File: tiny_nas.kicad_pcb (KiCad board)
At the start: 4 copper layers, 0 parts

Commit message: pcb component placement
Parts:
- added C1: 100n, Capacitor_SMD:C_0402_1005Metric, F.Cu at (128.8, 95.5)
- added C10: 100n, Capacitor_SMD:C_0402_1005Metric, F.Cu at (144.8, 73.4)
- added C11: 100n, Capacitor_SMD:C_0402_1005Metric, F.Cu at (137.9, 73.9)
- added C12: 100n, Capacitor_SMD:C_0402_1005Metric, F.Cu at (127.5, 93.0)
- added C13: 100n, Capacitor_SMD:C_0402_1005Metric, F.Cu at (132.1, 96.5)
- added C14: 22u, Capacitor_SMD:C_0805_2012Metric, F.Cu at (171.7, 124.2)
- added C15: 100n, Capacitor_SMD:C_0402_1005Metric, F.Cu at (130.0, 83.3)
- added C16: 100n, Capacitor_SMD:C_0402_1005Metric, F.Cu at (131.6, 88.1)
- added C17: 22u, Capacitor_SMD:C_0805_2012Metric, F.Cu at (172.5, 118.4)
- added C18: 100n, Capacitor_SMD:C_0402_1005Metric, F.Cu at (132.1, 94.5)
- added C19: 100n, Capacitor_SMD:C_0402_1005Metric, F.Cu at (139.7, 103.6)
- added C2: 4.7u, Capacitor_SMD:C_0603_1608Metric, F.Cu at (130.0, 82.0)
- added C20: 100n, Capacitor_SMD:C_0402_1005Metric, F.Cu at (146.1, 103.6)
- added C21: 100n, Capacitor_SMD:C_0402_1005Metric, F.Cu at (151.1, 103.9)
- added C22: 10p, Capacitor_SMD:C_0402_1005Metric, F.Cu at (121.7, 93.0)
- added C23: 10p, Capacitor_SMD:C_0402_1005Metric, F.Cu at (121.7, 91.4)
- added C24: 30p, Capacitor_SMD:C_0402_1005Metric, F.Cu at (103.6, 89.9)
- added C25: 30p, Capacitor_SMD:C_0402_1005Metric, F.Cu at (103.6, 80.8)
- added C26: 100n, Capacitor_SMD:C_0402_1005Metric, F.Cu at (124.5, 85.3)
- added C27: 470p, Capacitor_SMD:C_0402_1005Metric, F.Cu at (117.9, 80.8)
- added C28: 100n, Capacitor_SMD:C_0402_1005Metric, F.Cu at (146.3, 120.6)
- added C29: 1u, Capacitor_SMD:C_0603_1608Metric, F.Cu at (117.9, 81.8)
- added C3: 2.2u, Capacitor_SMD:C_0603_1608Metric, F.Cu at (155.7, 104.9)
- added C30: 4.7u, Capacitor_SMD:C_0603_1608Metric, F.Cu at (147.1, 107.7)
- added C31: 100n, Capacitor_SMD:C_0402_1005Metric, F.Cu at (128.5, 76.7)
- added C32: 100n, Capacitor_SMD:C_0402_1005Metric, F.Cu at (118.1, 77.0)
- added C33: 100n, Capacitor_SMD:C_0402_1005Metric, F.Cu at (142.7, 108.5)
- added C34: 100n, Capacitor_SMD:C_0402_1005Metric, F.Cu at (140.5, 108.7)
- added C35: 10u, Capacitor_SMD:C_0805_2012Metric, F.Cu at (114.6, 74.2)
- added C36: 100n, Capacitor_SMD:C_0402_1005Metric, F.Cu at (151.4, 120.1)
- added C37: 100n, Capacitor_SMD:C_0402_1005Metric, F.Cu at (149.6, 108.7)
- added C38: 4.7u, Capacitor_SMD:C_0603_1608Metric, F.Cu at (139.2, 108.7)
- added C39: 100n, Capacitor_SMD:C_0402_1005Metric, F.Cu at (147.8, 120.1)
- added C4: 100n, Capacitor_SMD:C_0402_1005Metric, F.Cu at (158.8, 101.9)
- added C40: 100n, Capacitor_SMD:C_0402_1005Metric, F.Cu at (136.1, 114.6)
- added C41: 100n, Capacitor_SMD:C_0402_1005Metric, F.Cu at (110.5, 72.6)
- added C42: 100n, Capacitor_SMD:C_0402_1005Metric, F.Cu at (142.0, 68.3)
- added C43: 100n, Capacitor_SMD:C_0402_1005Metric, F.Cu at (134.4, 70.4)
- added C44: 100n, Capacitor_SMD:C_0402_1005Metric, F.Cu at (113.8, 70.1)
- added C45: 100n, Capacitor_SMD:C_0402_1005Metric, F.Cu at (173.5, 115.8)
- added C46: 100n, Capacitor_SMD:C_0402_1005Metric, F.Cu at (168.4, 109.0)
- added C47: 4.7u, Capacitor_SMD:C_0603_1608Metric, F.Cu at (159.0, 118.6)
- added C48: 4.7u, Capacitor_SMD:C_0603_1608Metric, F.Cu at (162.3, 115.8)
- added C49: 33p, Capacitor_SMD:C_0402_1005Metric, F.Cu at (153.4, 108.7)
- added C5: 2.2u, Capacitor_SMD:C_0603_1608Metric, F.Cu at (163.8, 80.5)
- added C50: 33p, Capacitor_SMD:C_0402_1005Metric, F.Cu at (162.8, 108.7)
- added C6: 100n, Capacitor_SMD:C_0402_1005Metric, F.Cu at (163.3, 92.2)
- added C7: 100n, Capacitor_SMD:C_0402_1005Metric, F.Cu at (163.3, 86.9)
- added C8: 100n, Capacitor_SMD:C_0402_1005Metric, F.Cu at (160.5, 77.2)
- added C9: 100n, Capacitor_SMD:C_0402_1005Metric, F.Cu at (150.4, 73.4)
- added D1: LED, LED_SMD:LED_0603_1608Metric, F.Cu at (159.5, 124.5)
- added D2: LED, LED_SMD:LED_0603_1608Metric, F.Cu at (169.9, 101.6)
- added FB1: 600R, Inductor_SMD:L_0603_1608Metric, F.Cu at (138.7, 63.2)
- added FB2: 120R, Inductor_SMD:L_0603_1608Metric, F.Cu at (169.2, 92.5)
- added FB3: 120R, Inductor_SMD:L_0603_1608Metric, F.Cu at (133.9, 122.9)
- added J1: Conn_02x07_Odd_Even, Connector_PinHeader_1.27mm:PinHeader_2x07_P1.27mm_Vertical, F.Cu at (173.2, 61.7)
- added J2: DM3AT-SF-PEJM5, DM3AT-SF-PEJM5:HRS_DM3AT-SF-PEJM5, F.Cu at (113.0, 109.0)
- added J3: USB_B_Micro, Connector_USB:USB_Micro-B_Molex_47346-0001, F.Cu at (174.9, 87.4)
- added J4: Conn_01x02_Male, Connector_PinHeader_2.54mm:PinHeader_1x02_P2.54mm_Vertical, F.Cu at (124.7, 121.2)
- added J5: HR911105A, HR911105A:HANRUN_HR911105A, F.Cu at (124.0, 62.0)
- added J6: USB_B_Micro, Connector_USB:USB_Micro-B_Molex_47346-0001, F.Cu at (143.8, 124.2)
- added J7: USB_B_Micro, Connector_USB:USB_Micro-B_Molex_47346-0001, F.Cu at (175.0, 110.0)
- added J8: Conn_01x02_Male, Connector_PinHeader_2.54mm:PinHeader_1x02_P2.54mm_Vertical, F.Cu at (172.7, 78.0)
- added J9: Conn_01x02_Male, Connector_PinHeader_2.54mm:PinHeader_1x02_P2.54mm_Vertical, F.Cu at (151.6, 125.0)
- added JP1: SolderJumper_2_Bridged, Jumper:SolderJumper-2_P1.3mm_Bridged_RoundedPad1.0x1.5mm, F.Cu at (145.0, 107.7)
- added JP2: SolderJumper_2_Bridged, Jumper:SolderJumper-2_P1.3mm_Bridged_RoundedPad1.0x1.5mm, F.Cu at (145.5, 118.5)
- added R1: 4.7k, Resistor_SMD:R_0402_1005Metric, F.Cu at (158.5, 60.5)
- added R10: 33R, Resistor_SMD:R_0402_1005Metric, F.Cu at (125.2, 101.3)
- added R11: 33R, Resistor_SMD:R_0402_1005Metric, F.Cu at (128.3, 104.9)
- added R12: 33R, Resistor_SMD:R_0402_1005Metric, F.Cu at (128.3, 101.3)
- added R13: 33R, Resistor_SMD:R_0402_1005Metric, F.Cu at (131.1, 101.3)
- added R14: 0R, Resistor_SMD:R_0402_1005Metric, F.Cu at (131.1, 104.9)
- added R15: 47k, Resistor_SMD:R_0402_1005Metric, F.Cu at (116.1, 103.4)
- added R16: 47k, Resistor_SMD:R_0402_1005Metric, F.Cu at (113.0, 103.4)
- added R17: 47k, Resistor_SMD:R_0402_1005Metric, F.Cu at (110.0, 103.4)
- added R18: 47k, Resistor_SMD:R_0402_1005Metric, F.Cu at (106.9, 103.4)
- added R19: 100R, Resistor_SMD:R_0402_1005Metric, F.Cu at (108.5, 99.6)
- added R2: 1k5, Resistor_SMD:R_0402_1005Metric, F.Cu at (175.5, 121.9)
- added R20: 47k, Resistor_SMD:R_0402_1005Metric, F.Cu at (104.1, 103.4)
- added R21: 12.1k, Resistor_SMD:R_0402_1005Metric, F.Cu at (104.4, 99.6)
- added R22: 50R, Resistor_SMD:R_0402_1005Metric, F.Cu at (111.5, 78.5)
- added R23: 10k, Resistor_SMD:R_0402_1005Metric, F.Cu at (128.8, 85.6)
- added R24: 50R, Resistor_SMD:R_0402_1005Metric, F.Cu at (111.8, 81.0)
- added R25: 50R, Resistor_SMD:R_0402_1005Metric, F.Cu at (114.0, 86.6)
- added R26: 270R, Resistor_SMD:R_0402_1005Metric, F.Cu at (112.5, 55.1)
- added R27: 270R, Resistor_SMD:R_0402_1005Metric, F.Cu at (136.7, 55.4)
- added R28: 50R, Resistor_SMD:R_0402_1005Metric, F.Cu at (112.8, 83.8)
- added R29: 12k, Resistor_SMD:R_0402_1005Metric, F.Cu at (126.0, 109.7)
- added R3: 1k5, Resistor_SMD:R_0402_1005Metric, F.Cu at (173.2, 101.6)
- added R30: 820R, Resistor_SMD:R_0402_1005Metric, F.Cu at (133.3, 119.1)
- added R31: 100k, Resistor_SMD:R_0402_1005Metric, F.Cu at (159.3, 117.1)
- added R32: 1M, Resistor_SMD:R_0402_1005Metric, F.Cu at (159.0, 109.2)
- added R33: 0R, Resistor_SMD:R_0402_1005Metric, F.Cu at (135.4, 111.5)
- added R4: 10k, Resistor_SMD:R_0402_1005Metric, F.Cu at (104.9, 93.0)
- added R5: 10k, Resistor_SMD:R_0402_1005Metric, F.Cu at (107.7, 93.0)
- added R6: 10k, Resistor_SMD:R_0402_1005Metric, F.Cu at (110.7, 93.0)
- added R7: 1k5, Resistor_SMD:R_0402_1005Metric, F.Cu at (106.4, 96.0)
- added R8: 10k, Resistor_SMD:R_0402_1005Metric, F.Cu at (109.5, 96.0)
- added R9: 10k, Resistor_SMD:R_0402_1005Metric, F.Cu at (153.7, 71.9)
- added SW1: SW_SPDT, Button_Switch_SMD:SW_SPDT_PCM12, F.Cu at (168.1, 54.4)
- added U1: AMS1117-3.3, Package_TO_SOT_SMD:SOT-223-3_TabPin2, F.Cu at (165.6, 121.2)
- added U2: LAN8720A, Package_DFN_QFN:QFN-24-1EP_4x4mm_P0.5mm_EP2.6x2.6mm, F.Cu at (124.7, 80.5)
- added U3: STM32F407ZGTx, Package_QFP:LQFP-144_20x20mm_P0.5mm, F.Cu at (147.3, 88.9)
- added U4: USBLC6-4SC6, Package_TO_SOT_SMD:SOT-23-6, F.Cu at (105.3, 75.9)
- added U5: USB3300-EZK, Package_DFN_QFN:QFN-32-1EP_5x5mm_P0.5mm_EP3.45x3.45mm, F.Cu at (143.5, 113.9)
- added U6: MAX1823BEUB, MAX1823BEUB_T:SOP50P490X110-10N, F.Cu at (151.1, 117.3)
- added U7: CH340E, Package_SO:MSOP-10_3x3mm_P0.5mm, F.Cu at (168.3, 113.0)
- added Y1: 16MHz, Crystal:Crystal_SMD_3225-4Pin_3.2x2.5mm, F.Cu at (117.6, 92.2)
- added Y2: 25MHz, Crystal:Crystal_HC49-U_Vertical, F.Cu at (106.7, 87.8)
- added Y3: 24MHz, Crystal:Crystal_HC49-U_Vertical, F.Cu at (154.3, 112.5)
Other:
- board outline added: 76.2 x 76.2 mm

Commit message: route USB3300
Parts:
- moved R3 40.1 mm to (167.1, 62.0)
- moved D2 40.1 mm to (163.8, 62.0)
- moved U6 24.6 mm to (167.9, 99.3)
- moved C49 24.1 mm to (177.0, 104.1), turned to -90 degrees
- moved Y3 22.5 mm to (174.0, 101.8), turned to 90 degrees
- moved C50 20.7 mm to (176.8, 93.5), turned to 90 degrees
- moved U4 19.5 mm to (124.7, 74.4)
- moved R2 19.0 mm to (156.7, 124.5)
- moved JP2 18.9 mm to (162.3, 109.7)
- moved FB1 16.6 mm to (131.1, 78.0), turned to 90 degrees
- moved JP1 14.5 mm to (159.5, 109.0), turned to 180 degrees
- moved C30 12.8 mm to (159.5, 110.7), turned to 180 degrees
- moved R32 11.7 mm to (169.9, 105.2), turned to 90 degrees
- moved C28 8.67 mm to (154.9, 119.9)
- moved C39 3.09 mm to (149.1, 123.0)
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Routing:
- net +3V3: track 0.00 -> 187.1 mm, vias 0 -> 3
- net /ULPI_RESET: track 0.00 -> 69.5 mm
- net Net-(R31-Pad1): track 0.00 -> 69.4 mm, vias 0 -> 8
- net Net-(U5-Pad3): track 0.00 -> 60.0 mm, vias 0 -> 2
- net /ULPI_STP: track 0.00 -> 59.3 mm, vias 0 -> 2
- net Net-(J4-Pad1): track 0.00 -> 56.5 mm, vias 0 -> 4
- net Net-(R30-Pad1): track 0.00 -> 56.1 mm, vias 0 -> 6
- net /ULPI_DIR: track 0.00 -> 55.4 mm, vias 0 -> 2
- net /ULPI_D7: track 0.00 -> 55.0 mm, vias 0 -> 2
- net /ULPI_NXT: track 0.00 -> 52.4 mm, vias 0 -> 2
- net GND: track 0.00 -> 49.0 mm, vias 0 -> 9
- net /ETH_TX-: track 0.00 -> 48.0 mm
- net Net-(C50-Pad1): track 0.00 -> 47.0 mm, vias 0 -> 6
- net /ETH_TX+: track 0.00 -> 45.4 mm
- net Net-(C49-Pad1): track 0.00 -> 44.4 mm, vias 0 -> 6
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- added copper zone on In1.Cu, net GND
- added copper zone on In2.Cu, net GND

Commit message: route all
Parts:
- moved R19 65.9 mm to (166.6, 68.6)
- moved R9 32.5 mm to (125.2, 87.6), turned to 180 degrees
- moved R28 30.9 mm to (139.2, 67.8), turned to 180 degrees
- moved R25 29.9 mm to (138.4, 69.3), turned to 180 degrees
- moved R11 21.4 mm to (110.2, 93.5), turned to 180 degrees
- moved R14 19.3 mm to (113.8, 96.3)
- moved R24 13.0 mm to (111.0, 68.1)
- moved R22 12.7 mm to (111.0, 65.8)
- moved R23 10.0 mm to (118.9, 87.1)
- moved C43 6.18 mm to (135.4, 76.5)
- moved C50 4.07 mm to (177.0, 97.5), turned to -90 degrees
- moved R12 3.87 mm to (126.7, 97.8), turned to 180 degrees
- moved C49 3.56 mm to (177.0, 100.6), turned to 90 degrees
- moved C37 3.06 mm to (147.3, 110.7)
- moved C11 2.18 mm to (139.7, 75.2)
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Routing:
- net +3V3: track 187.1 -> 542.6 mm, vias 3 -> 26
- net Net-(U3-Pad114): track 0.00 -> 139.1 mm, vias 0 -> 4
- net GND: track 49.0 -> 178.5 mm, vias 9 -> 59
- net Net-(C31-Pad1): track 0.00 -> 118.6 mm, vias 0 -> 4
- net Net-(C12-Pad2): track 0.00 -> 92.8 mm, vias 0 -> 8
- net Net-(J5-Pad9): track 0.00 -> 91.5 mm, vias 0 -> 2
- net /SDIO_CK: track 0.00 -> 77.1 mm, vias 0 -> 6
- net /USART_RX: track 0.00 -> 74.3 mm, vias 0 -> 4
- net /SDIO_CMD: track 0.00 -> 72.7 mm, vias 0 -> 8
- net Net-(J5-Pad12): track 0.00 -> 72.7 mm, vias 0 -> 2
- net /SDIO_D1: track 0.00 -> 71.7 mm, vias 0 -> 4
- net /SDIO_D0: track 0.00 -> 68.9 mm, vias 0 -> 6
- net /SDIO_D3: track 0.00 -> 68.4 mm, vias 0 -> 6
- net /USART_TX: track 0.00 -> 68.3 mm, vias 0 -> 8
- net Net-(U3-Pad115): track 0.00 -> 68.1 mm, vias 0 -> 2
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
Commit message: passed DRC
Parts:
- moved C49 7.98 mm to (175.8, 92.7), turned to 180 degrees
- moved C50 6.48 mm to (172.7, 92.7), turned to 0 degrees
- moved C24 2.58 mm to (103.4, 92.5)
- moved C25 2.54 mm to (105.2, 78.7), turned to 0 degrees
- moved R6 1.14 mm to (111.3, 92.2)
- moved C1 0.76 mm to (128.8, 96.3)
- moved C36 0.38 mm to (151.6, 119.9), turned to 180 degrees
- moved C30 0.37 mm to (159.3, 111.0)
- moved C27 0.36 mm to (117.6, 80.5)
- moved JP2 0.36 mm to (162.6, 109.5)
- moved R4 0.25 mm to (105.2, 93.0)
- moved U4 0.25 mm to (124.7, 74.9)
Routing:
- net GND: track 178.5 -> 191.9 mm, vias 59 -> 63
- net Net-(C49-Pad1): track 47.8 -> 54.8 mm
- net Net-(C50-Pad1): track 46.3 -> 53.3 mm
- net +3V3: track 542.6 -> 548.9 mm, vias 26 -> 27
- net Net-(C25-Pad1): track 25.6 -> 29.1 mm
- net Net-(C24-Pad1): track 29.0 -> 31.5 mm
- net Net-(C28-Pad1): track 21.4 -> 23.0 mm
- net Net-(R11-Pad2): track 27.0 -> 25.7 mm
- net Net-(R31-Pad1): track 92.3 -> 91.4 mm
- net Net-(R12-Pad1): track 33.7 -> 32.9 mm
- net VBUS: track 71.7 -> 71.0 mm
- net /ULPI_DIR: track 58.3 -> 57.6 mm
- net Net-(R13-Pad1): track 24.3 -> 23.7 mm
- net /ETH_RX-: track 42.0 -> 41.5 mm

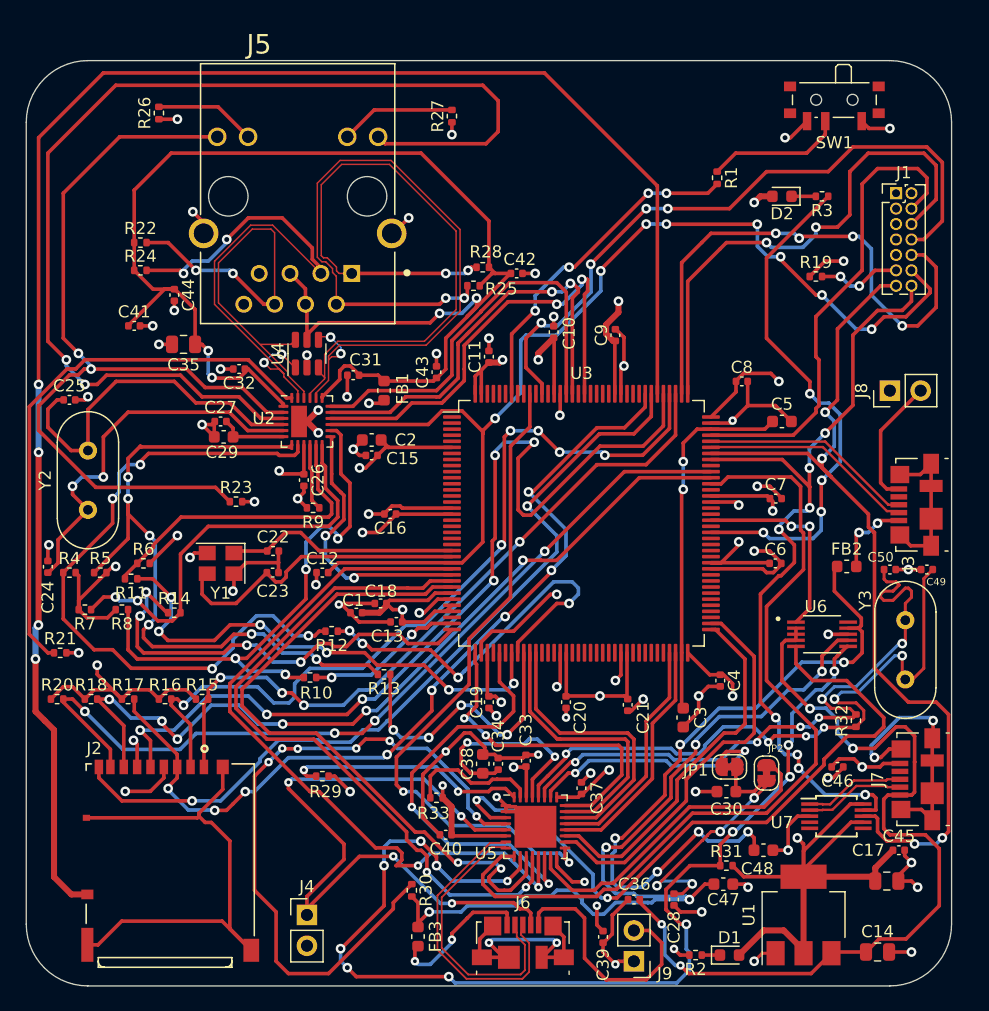
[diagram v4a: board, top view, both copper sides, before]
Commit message: Added Ethernet PHY reset GPIO and pin header to choose input clock from MCO or crystal
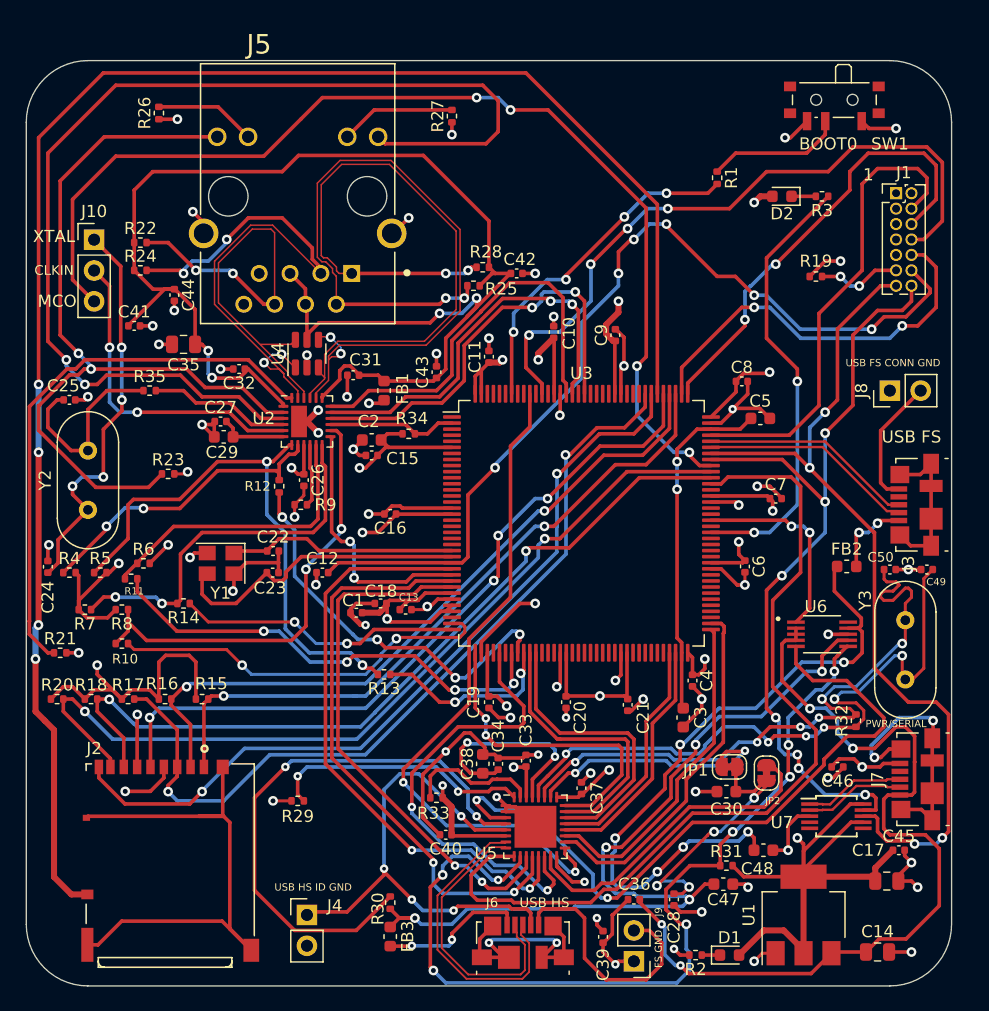
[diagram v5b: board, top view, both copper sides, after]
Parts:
- added J10: Conn_01x03_Male, Connector_PinHeader_2.54mm:PinHeader_1x03_P2.54mm_Vertical, F.Cu at (107.2, 65.5)
- added R34: 4k7, Resistor_SMD:R_0402_1005Metric, F.Cu at (133.1, 81.5)
- added R35: 0R, Resistor_SMD:R_0402_1005Metric, F.Cu at (111.8, 78.0)
- Y1: value 16MHz -> 25MHz
- moved R10 15.7 mm to (109.5, 98.8)
- moved R12 12.7 mm to (122.4, 85.9), turned to 90 degrees
- moved R23 6.04 mm to (113.3, 84.8)
- moved R29 2.87 mm to (124.0, 111.8), turned to 180 degrees
- moved C6 2.52 mm to (160.8, 92.5), turned to -90 degrees
- moved C4 2.29 mm to (156.5, 101.9)
- moved FB3 2.29 mm to (131.6, 122.9)
- moved R30 2.05 mm to (131.6, 120.1)
- moved C5 1.80 mm to (162.1, 80.3)
- moved C13 1.27 mm to (132.8, 96.0), turned to 0 degrees
- moved R14 1.08 mm to (114.6, 95.5), turned to 180 degrees
- moved R9 1.05 mm to (124.2, 87.4)
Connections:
- net Net-(R10-Pad1) renamed /PHY_REFCLK_MCU
- net Net-(R10-Pad2) renamed /PHY_REFCLK
- net Net-(R11-Pad1) renamed /PHY_CRSDV_MCU
- net Net-(R11-Pad2) renamed /PHY_CRSDV
- net Net-(R12-Pad1) renamed /PHY_RXD0_MCU
- net Net-(R12-Pad2) renamed /PHY_RXD0
- net Net-(R13-Pad1) renamed /PHY_RXD1_MCU
- net Net-(R13-Pad2) renamed /PHY_RXD1
- net Net-(R14-Pad1) renamed /PHY_MDIO_MCU
- net Net-(R14-Pad2) renamed /PHY_MDIO
- net Net-(R9-Pad1) renamed /PHY_RXER
- net Net-(U2-Pad13) renamed /PHY_MDC
- net Net-(U2-Pad16) renamed /PHY_TXEN
- net Net-(U2-Pad17) renamed /PHY_TXD0
- net Net-(U2-Pad18) renamed /PHY_TXD1
- U2 pad 15: Net-(C12-Pad2) -> /PHY_RST
- U2 pad 4: Net-(C25-Pad1) -> Net-(R35-Pad2)
- U2 pad 5: Net-(C24-Pad1) -> Net-(J10-Pad2)
- U3 pad 100: unconnected-(U3-Pad100) -> Net-(J10-Pad3)
- U3 pad 2: unconnected-(U3-Pad2) -> /PHY_RST
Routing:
- net Net-(J10-Pad3): track 0.00 -> 89.0 mm, vias 0 -> 4
- net /PHY_RXD0: track 56.3 -> 25.9 mm, vias 4 -> 2
- net Net-(J10-Pad2): track 0.00 -> 26.7 mm, vias 0 -> 2
- net +3V3: track 548.9 -> 528.4 mm
- net /PHY_REFCLK_MCU: track 13.0 -> 32.1 mm
- net Net-(C12-Pad2): track 92.8 -> 76.3 mm, vias 8 -> 6
- net /SDIO_CK: track 77.1 -> 61.0 mm, vias 6 -> 4
- net Net-(R31-Pad1): track 91.4 -> 75.7 mm, vias 12 -> 8
- net Net-(J4-Pad1): track 57.5 -> 42.4 mm
- net Net-(C25-Pad1): track 29.1 -> 15.8 mm
- net /PHY_RXD1: track 58.8 -> 45.9 mm, vias 6 -> 2
- net /PHY_MDIO_MCU: track 36.3 -> 23.4 mm, vias 4 -> 2
- net /ULPI_NXT: track 56.1 -> 44.0 mm
- net Net-(R35-Pad2): track 0.00 -> 11.7 mm
- net Net-(J1-Pad10): track 44.7 -> 33.0 mm, vias 4 -> 2
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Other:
- board text added: "1"
- board text added: "BOOT0"
- board text added: "CLKIN"
- board text added: "FS GND"
- board text added: "MCO"
- board text added: "PWR/SERIAL"
- board text added: "USB FS"
- board text added: "USB FS CONN GND"
- board text added: "USB HS"
- board text added: "USB HS ID GND"
- board text added: "XTAL"

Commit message: change resistors footprint, add manufacturing files
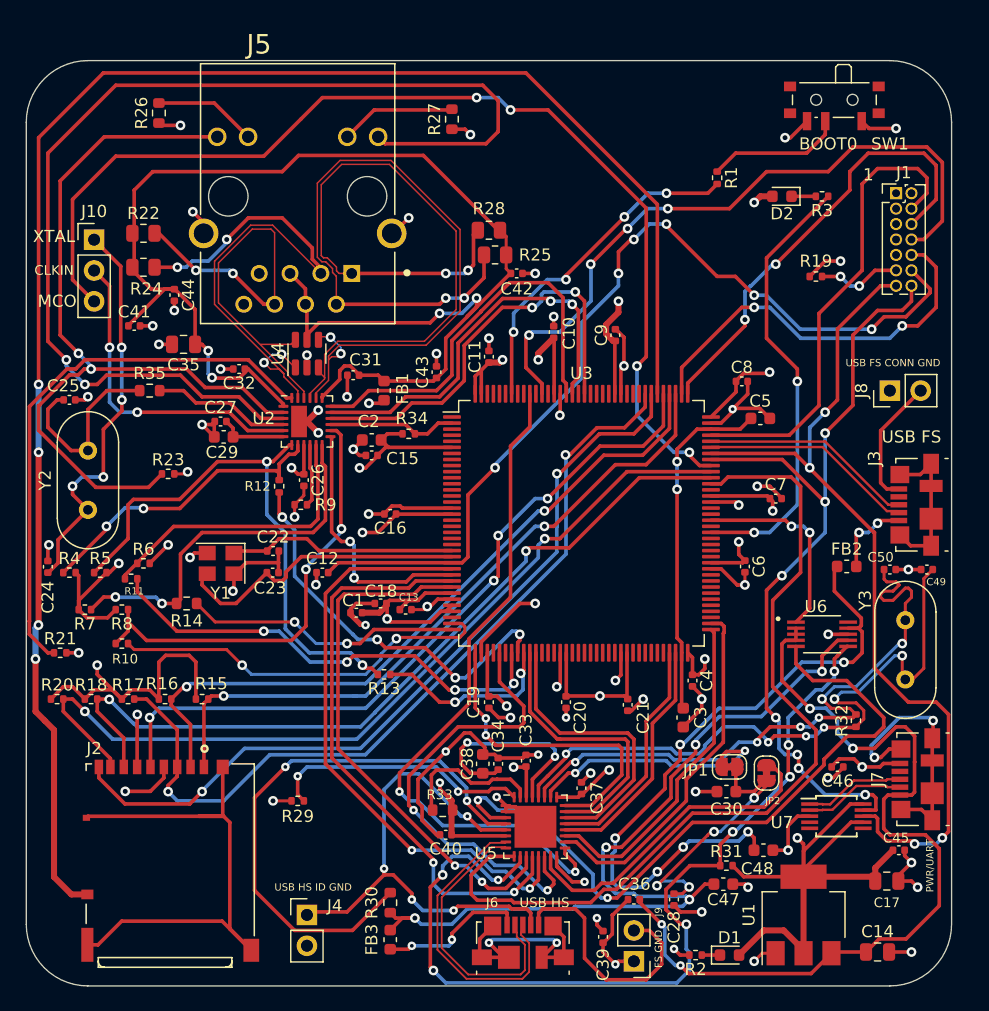
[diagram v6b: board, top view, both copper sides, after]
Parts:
- R14, R26, R27, R30, R33, R35: footprint Resistor_SMD:R_0402_1005Metric -> Resistor_SMD:R_0603_1608Metric
- R22, R24, R25, R28: value 50R -> 49.9R; footprint Resistor_SMD:R_0402_1005Metric -> Resistor_SMD:R_0805_2012Metric
- moved R25 3.10 mm to (140.2, 66.8)
- moved R28 3.09 mm to (139.7, 64.8)
- moved R33 1.14 mm to (135.9, 112.5)
- moved R22 0.80 mm to (111.3, 65.0)
- moved R24 0.36 mm to (111.3, 67.8)
- moved R14 0.25 mm to (114.8, 95.5)
- moved R27 0.25 mm to (136.7, 55.6)
- moved FB3 0.25 mm to (131.6, 123.2)
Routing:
- net /ETH_TX-: track 64.5 -> 67.6 mm
- net /ETH_TX+: track 57.6 -> 60.5 mm
- net Net-(C31-Pad1): track 117.9 -> 115.7 mm
- net GND: track 185.2 -> 186.8 mm
- net /ETH_RX+: track 50.5 -> 49.3 mm
- net Net-(R33-Pad1): track 11.0 -> 12.0 mm
- net /ULPI_D7: track 55.8 -> 56.7 mm
- net /PHY_MDIO_MCU: track 23.4 -> 22.9 mm
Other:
- board text added: "PWR/UART"
- board text removed: "PWR/SERIAL"
